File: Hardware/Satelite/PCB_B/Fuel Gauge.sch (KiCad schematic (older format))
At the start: 5 parts, among them U9 BQ27441DRZR-G1A

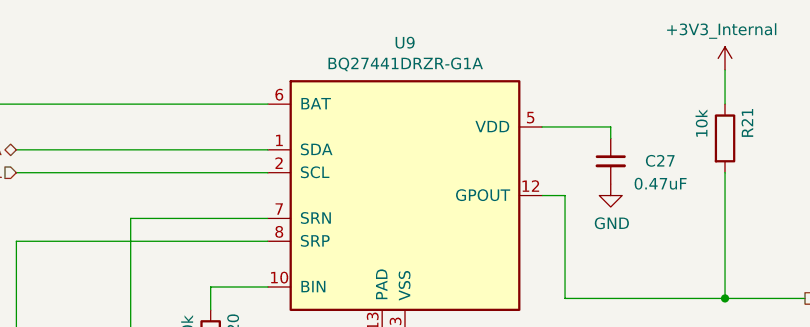
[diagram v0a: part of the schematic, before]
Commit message: Añadida información faltante en rótulos de los esquemas
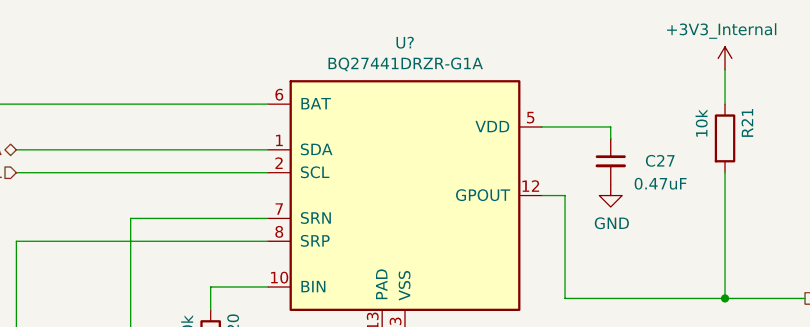
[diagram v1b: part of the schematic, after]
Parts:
- renumbered U9 to U?
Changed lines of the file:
@@
 encoding utf-8
 Sheet 6 6
-Title ""
-Date ""
-Rev ""
+Title "Fuel gauge"
+Date "2019-01-19"
+Rev "1.0.0"
 Comp ""
 Comment1 ""
@@
 $EndDescr
 $Comp
-L Battery_Management:BQ27441DRZR-G1A U9
+L Battery_Management:BQ27441DRZR-G1A U?
 U 1 1 5BB27F17
 P 5900 3700
-F 0 "U9" H 5900 4367 50  0000 C CNN
+F 0 "U?" H 5900 4367 50  0000 C CNN
 F 1 "BQ27441DRZR-G1A" H 5900 4276 50  0000 C CNN
 F 2 "Package_SON:Texas_S-PDSO-N12" H 6150 3150 50  0001 L CNN
